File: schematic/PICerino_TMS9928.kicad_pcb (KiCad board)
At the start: 2 copper layers, 105 x 112.9 mm, 75 parts, among them CON1 PICERINO-EDGE, IC1 ADG453/413, IC2 AD813ANZ, J1 Conn_01x03, J10 Conn_01x03, J2 Conn_01x03, J3 Conn_01x02, J4 Conn_01x03, J5 Conn_01x03_Yb, J6 Conn_01x03_Y, J7 Conn_01x03_Yr, J8 Conn_01x08, J9 Conn_01x08, U1 LM1881, Y1 Crystal

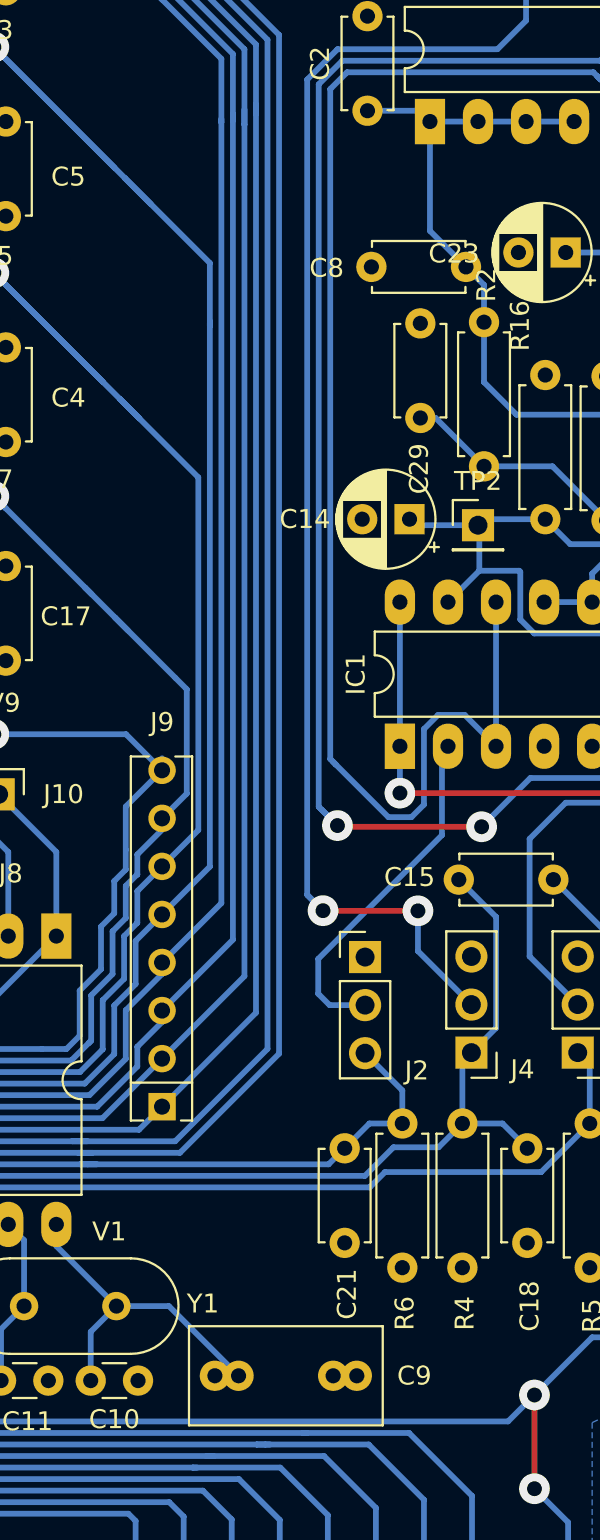
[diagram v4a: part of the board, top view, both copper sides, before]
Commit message: updated variable capacitor pads to be a bit larger
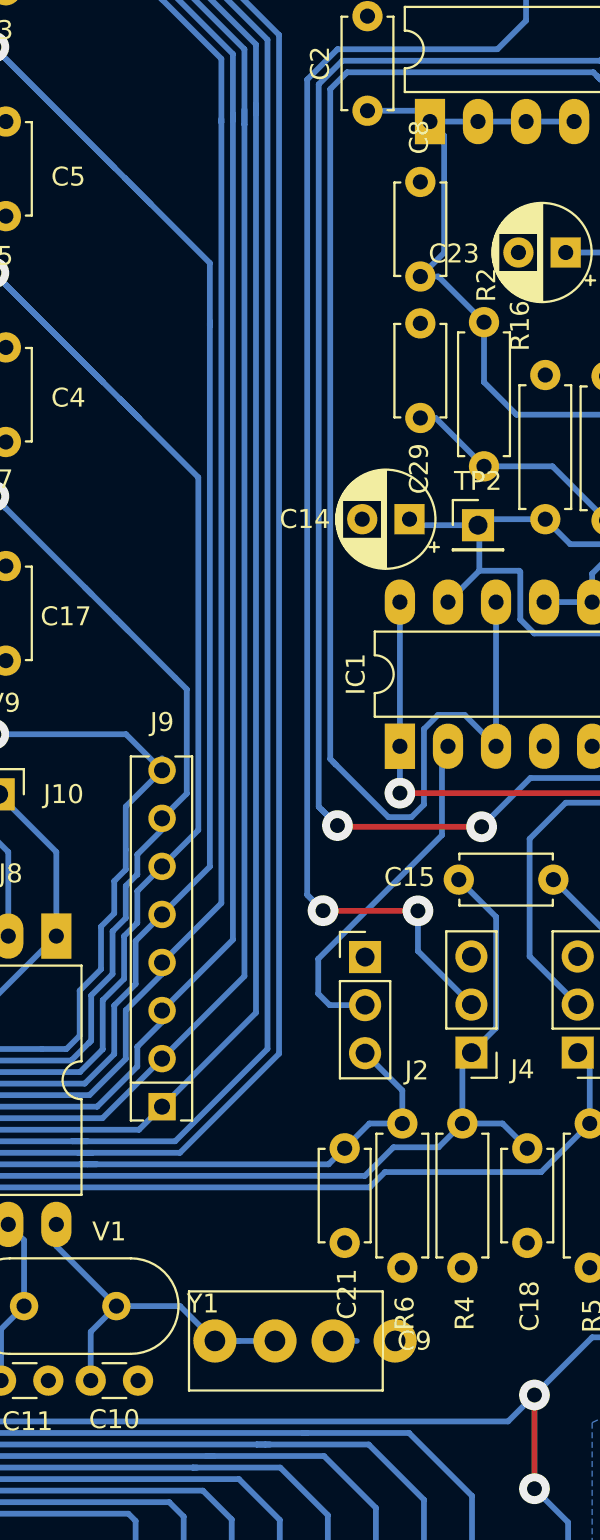
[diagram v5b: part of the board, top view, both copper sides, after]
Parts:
- moved C8 2.47 mm to (185.5, 76.3), turned to 90 degrees
- moved C9 1.84 mm to (174.6, 132.5)
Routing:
- net VCC: track 645.5 -> 647.1 mm
- net VSS: track 29.0 -> 30.2 mm
- net Net-(C10-Pad2): track 19.4 -> 20.5 mm

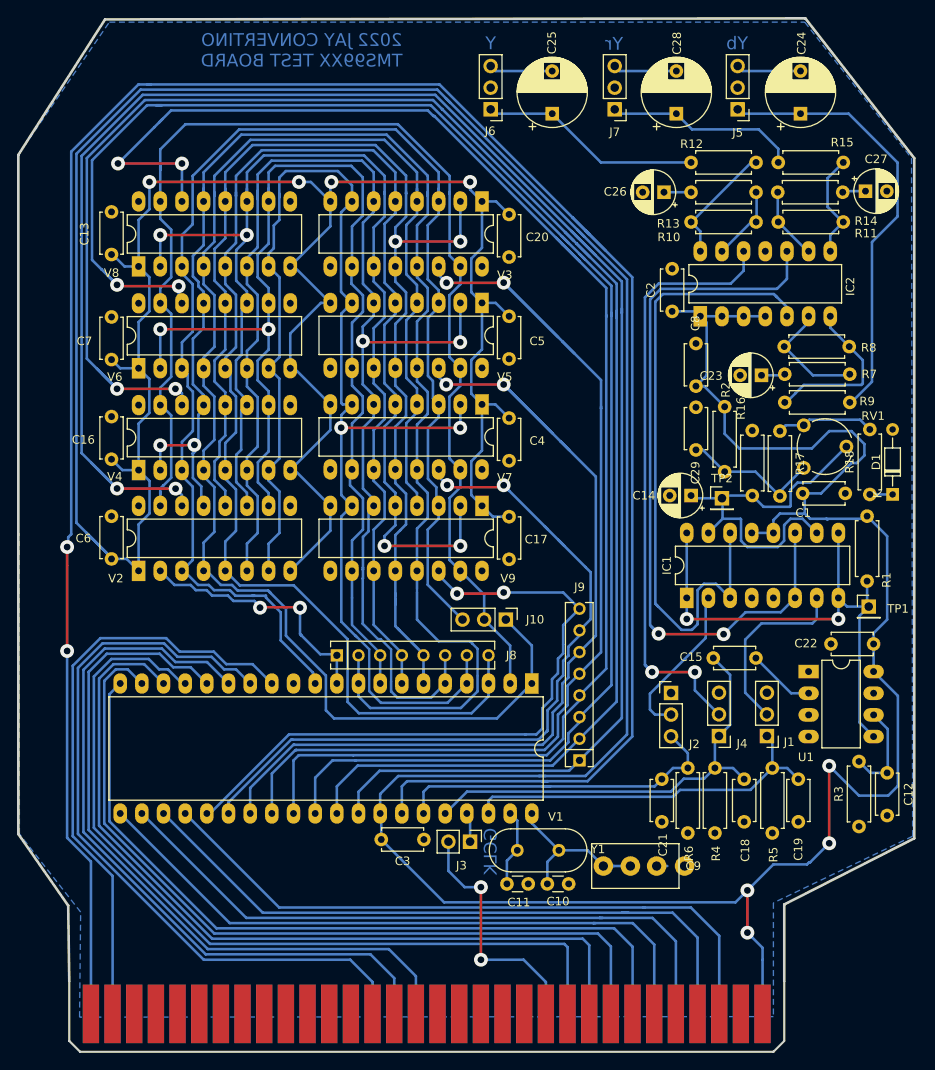
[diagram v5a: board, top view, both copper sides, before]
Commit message: using new kicad 6.X, changed files and includes a backup of the old project
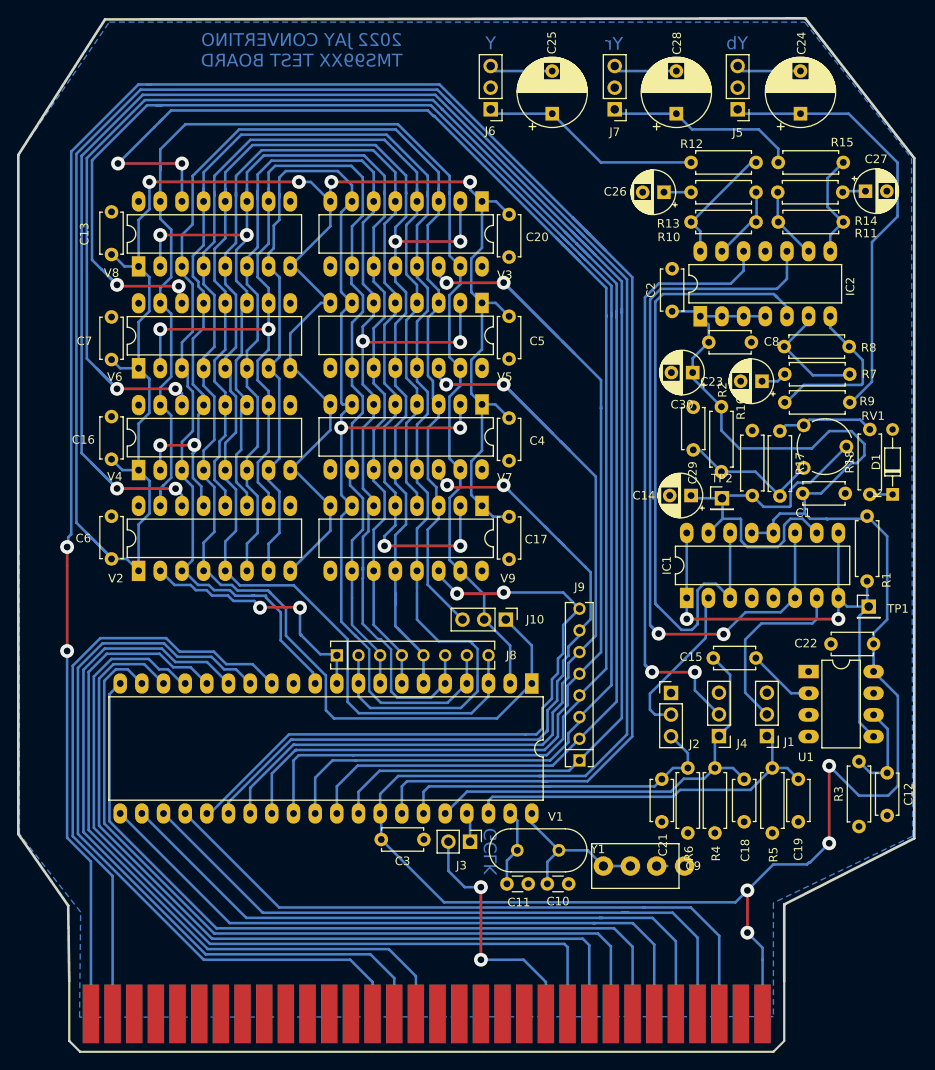
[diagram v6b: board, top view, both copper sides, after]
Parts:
- added C30: 10uF, Capacitor_THT:CP_Radial_D5.0mm_P2.50mm, F.Cu at (185.1, 74.7)
- moved C8 5.36 mm to (187.0, 71.1), turned to 0 degrees
- moved C23 0.70 mm to (193.2, 75.7)
- moved R2 0.38 mm to (188.5, 86.3)
- moved C29 0.32 mm to (185.2, 78.7)
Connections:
- CON1 pad A10: Net-(CON1-PadA10) -> unconnected-(CON1-PadA10)
- CON1 pad A11: Net-(CON1-PadA11) -> unconnected-(CON1-PadA11)
- CON1 pad A12: Net-(CON1-PadA12) -> unconnected-(CON1-PadA12)
- CON1 pad A13: Net-(CON1-PadA13) -> unconnected-(CON1-PadA13)
- CON1 pad A17: Net-(CON1-PadA17) -> unconnected-(CON1-PadA17)
- CON1 pad A18: Net-(CON1-PadA18) -> unconnected-(CON1-PadA18)
- CON1 pad A19: Net-(CON1-PadA19) -> unconnected-(CON1-PadA19)
- CON1 pad A20: Net-(CON1-PadA20) -> unconnected-(CON1-PadA20)
- CON1 pad A21: Net-(CON1-PadA21) -> unconnected-(CON1-PadA21)
- CON1 pad A3: Net-(CON1-PadA3) -> unconnected-(CON1-PadA3)
- CON1 pad A4: Net-(CON1-PadA4) -> unconnected-(CON1-PadA4)
- CON1 pad A5: Net-(CON1-PadA5) -> unconnected-(CON1-PadA5)
- CON1 pad A6: Net-(CON1-PadA6) -> unconnected-(CON1-PadA6)
- CON1 pad A7: Net-(CON1-PadA7) -> unconnected-(CON1-PadA7)
- CON1 pad A8: Net-(CON1-PadA8) -> unconnected-(CON1-PadA8)
- CON1 pad A9: Net-(CON1-PadA9) -> unconnected-(CON1-PadA9)
- CON1 pad B1: Net-(CON1-PadB1) -> unconnected-(CON1-PadB1)
- CON1 pad B10: Net-(CON1-PadB10) -> unconnected-(CON1-PadB10)
- CON1 pad B11: Net-(CON1-PadB11) -> unconnected-(CON1-PadB11)
- CON1 pad B12: Net-(CON1-PadB12) -> unconnected-(CON1-PadB12)
- CON1 pad B13: Net-(CON1-PadB13) -> unconnected-(CON1-PadB13)
- CON1 pad B14: Net-(CON1-PadB14) -> unconnected-(CON1-PadB14)
- CON1 pad B15: Net-(CON1-PadB15) -> unconnected-(CON1-PadB15)
- CON1 pad B16: Net-(CON1-PadB16) -> unconnected-(CON1-PadB16)
- CON1 pad B17: Net-(CON1-PadB17) -> unconnected-(CON1-PadB17)
- CON1 pad B18: Net-(CON1-PadB18) -> unconnected-(CON1-PadB18)
- CON1 pad B19: Net-(CON1-PadB19) -> unconnected-(CON1-PadB19)
- CON1 pad B2: Net-(CON1-PadB2) -> unconnected-(CON1-PadB2)
- CON1 pad B20: Net-(CON1-PadB20) -> unconnected-(CON1-PadB20)
- CON1 pad B21: Net-(CON1-PadB21) -> unconnected-(CON1-PadB21)
- CON1 pad B22: Net-(CON1-PadB22) -> unconnected-(CON1-PadB22)
- CON1 pad B23: Net-(CON1-PadB23) -> unconnected-(CON1-PadB23)
- CON1 pad B24: Net-(CON1-PadB24) -> unconnected-(CON1-PadB24)
- CON1 pad B25: Net-(CON1-PadB25) -> unconnected-(CON1-PadB25)
- CON1 pad B26: Net-(CON1-PadB26) -> unconnected-(CON1-PadB26)
- CON1 pad B27: Net-(CON1-PadB27) -> unconnected-(CON1-PadB27)
- CON1 pad B28: Net-(CON1-PadB28) -> unconnected-(CON1-PadB28)
- CON1 pad B29: Net-(CON1-PadB29) -> unconnected-(CON1-PadB29)
- CON1 pad B3: Net-(CON1-PadB3) -> unconnected-(CON1-PadB3)
- CON1 pad B30: Net-(CON1-PadB30) -> unconnected-(CON1-PadB30)
- CON1 pad B31: Net-(CON1-PadB31) -> unconnected-(CON1-PadB31)
- CON1 pad B32: Net-(CON1-PadB32) -> unconnected-(CON1-PadB32)
- CON1 pad B4: Net-(CON1-PadB4) -> unconnected-(CON1-PadB4)
- CON1 pad B5: Net-(CON1-PadB5) -> unconnected-(CON1-PadB5)
- CON1 pad B6: Net-(CON1-PadB6) -> unconnected-(CON1-PadB6)
- CON1 pad B7: Net-(CON1-PadB7) -> unconnected-(CON1-PadB7)
- CON1 pad B8: Net-(CON1-PadB8) -> unconnected-(CON1-PadB8)
- CON1 pad B9: Net-(CON1-PadB9) -> unconnected-(CON1-PadB9)
- U1 pad 1: Net-(U1-Pad1) -> unconnected-(U1-Pad1)
- U1 pad 3: Net-(U1-Pad3) -> unconnected-(U1-Pad3)
- U1 pad 7: Net-(U1-Pad7) -> unconnected-(U1-Pad7)
- V2 pad 9: Net-(V2-Pad9) -> unconnected-(V2-Pad9)
- V3 pad 9: Net-(V3-Pad9) -> unconnected-(V3-Pad9)
- V4 pad 9: Net-(V4-Pad9) -> unconnected-(V4-Pad9)
- V5 pad 9: Net-(V5-Pad9) -> unconnected-(V5-Pad9)
- V6 pad 9: Net-(V6-Pad9) -> unconnected-(V6-Pad9)
- V7 pad 9: Net-(V7-Pad9) -> unconnected-(V7-Pad9)
- V8 pad 9: Net-(V8-Pad9) -> unconnected-(V8-Pad9)
- V9 pad 9: Net-(V9-Pad9) -> unconnected-(V9-Pad9)
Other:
- net class Default removed
